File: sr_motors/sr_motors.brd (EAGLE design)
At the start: 78.4 x 64.8 mm, 20 parts

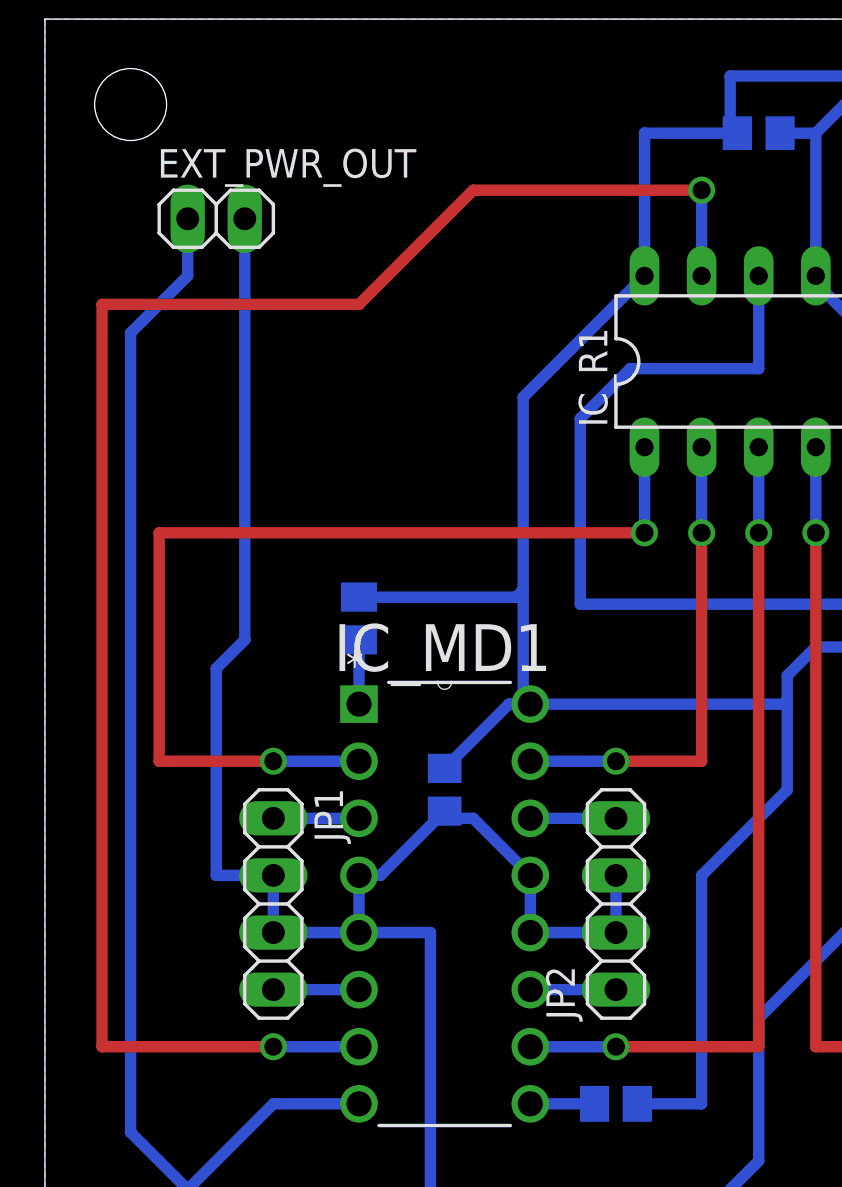
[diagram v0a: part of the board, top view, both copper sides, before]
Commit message: DRC and align: Set the same DRC for lights and motors, fixed new DRC errors in sr_lights, aligned headers
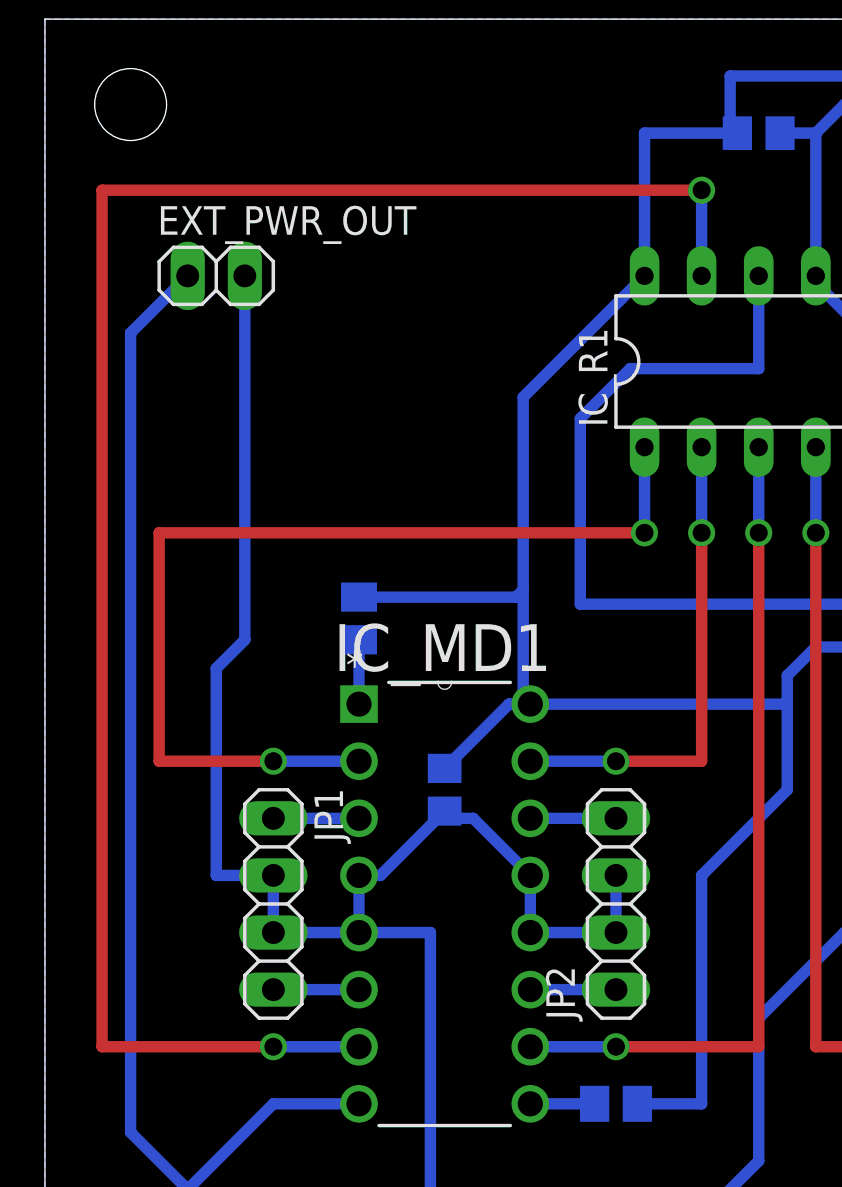
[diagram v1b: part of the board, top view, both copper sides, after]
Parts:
- moved EXT_PWR_OUT 2.54 mm to (7.62, 53.3)
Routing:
- net Q0: track 77.0 -> 80.0 mm
- net VCC2: track 101.8 -> 99.2 mm
- net GND: track 290.3 -> 287.8 mm
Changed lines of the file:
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@@
 </element>
 <element name="EXT_PWR_IN" library="pinhead" package="1X02" value="" x="7.62" y="8.89"/>
-<element name="EXT_PWR_OUT" library="pinhead" package="1X02" value="" x="7.62" y="55.88"/>
+<element name="EXT_PWR_OUT" library="pinhead" package="1X02" value="" x="7.62" y="53.34"/>
 <element name="IC_MD1" library="Texas Instruments_By_element14_Batch_1" package="DIP254P762X508-16" value="L293DNE" x="21.59" y="16.51">
 <attribute name="MPN" value="L293DNE" x="21.59" y="16.51" size="1.778" layer="27" display="off"/>
@@
 <wire x1="69.85" y1="24.13" x2="69.85" y2="53.34" width="0.508" layer="16"/>
 <wire x1="10.16" y1="26.67" x2="10.16" y2="24.13" width="0.508" layer="16"/>
-<wire x1="8.89" y1="37.1475" x2="8.89" y2="55.88" width="0.508" layer="16"/>
+<wire x1="8.89" y1="37.1475" x2="8.89" y2="53.34" width="0.508" layer="16"/>
 <wire x1="7.62" y1="35.8775" x2="8.89" y2="37.1475" width="0.508" layer="16"/>
 <wire x1="7.62" y1="26.67" x2="7.62" y2="35.8775" width="0.508" layer="16"/>
@@
 <wire x1="31.75" y1="13.97" x2="29.21" y2="11.43" width="0.508" layer="16"/>
 <wire x1="29.21" y1="11.43" x2="17.145" y2="11.43" width="0.508" layer="16"/>
-<polygon width="0.4064" layer="16">
+<polygon width="0.508" layer="16">
 <vertex x="0" y="64.77"/>
 <vertex x="78.74" y="64.77"/>
@@
 <via x="29.21" y="57.15" extent="1-16" drill="0.8" shape="square"/>
 <wire x1="10.16" y1="19.05" x2="2.54" y2="19.05" width="0.508" layer="1"/>
-<wire x1="2.54" y1="19.05" x2="2.54" y2="52.07" width="0.508" layer="1"/>
-<wire x1="2.54" y1="52.07" x2="13.97" y2="52.07" width="0.508" layer="1"/>
-<wire x1="13.97" y1="52.07" x2="19.05" y2="57.15" width="0.508" layer="1"/>
-<wire x1="19.05" y1="57.15" x2="29.21" y2="57.15" width="0.508" layer="1"/>
+<wire x1="2.54" y1="19.05" x2="2.54" y2="57.15" width="0.508" layer="1"/>
+<wire x1="2.54" y1="57.15" x2="29.21" y2="57.15" width="0.508" layer="1"/>
 </signal>
 <signal name="Q1">
@@
 <wire x1="16.51" y1="4.1275" x2="29.5275" y2="4.1275" width="0.508" layer="16"/>
 <wire x1="16.51" y1="4.1275" x2="16.51" y2="3.81" width="0.508" layer="16"/>
-<wire x1="6.35" y1="55.88" x2="6.35" y2="53.34" width="0.508" layer="16"/>
 <wire x1="6.35" y1="53.34" x2="3.81" y2="50.8" width="0.508" layer="16"/>
 <wire x1="3.81" y1="50.8" x2="3.81" y2="15.24" width="0.508" layer="16"/>

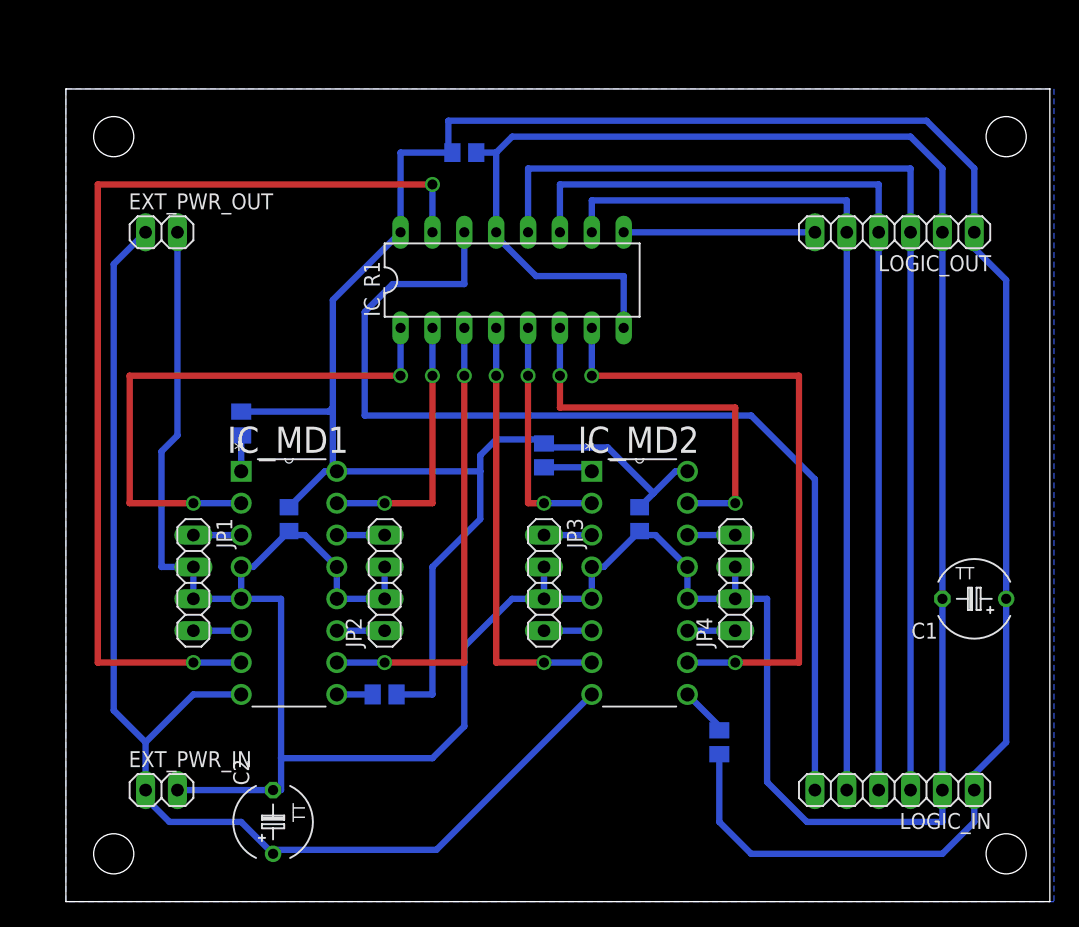
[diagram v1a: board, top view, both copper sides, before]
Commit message: Verion 1.2: Increased route width and board width, small other changes
Squashed commit of the following:

commit cb5b4ae53fc73325e271569d8207a4f4cb0d995e
Author: Sergey Kostyuk <contact@s-kostyuk.me>
Date:   Tue Sep 13 19:34:33 2016 +0300

    Increaded width of routes, increased board width, replaced capacitor package, updated board version

commit 30ef558f6f82cadcaf764826f9decc7df1a17ce0
Author: Sergey Kostyuk <contact@s-kostyuk.me>
Date:   Tue Sep 13 19:27:19 2016 +0300

    Replaced capacitor package

commit a2d398c50457a8d09da237926f830a1984b8064b
Author: Sergey Kostyuk <contact@s-kostyuk.me>
Date:   Tue Sep 13 18:08:38 2016 +0300

    Icreased width of routes, icreased board width

commit f5951c6459f5b93fe179c3fabd85f49e6b5260dd
Author: Sergey Kostyuk <contact@s-kostyuk.me>
Date:   Wed Sep 7 16:51:49 2016 +0300

    Increased width of power lines on sr_motors

commit 1e2f38b3539c2f4abccb8c8183ef937e4e63213c
Author: Sergey Kostyuk <ks.hot.ua@gmail.com>
Date:   Mon Aug 22 15:17:33 2016 +0300

    Added reverse current protection for external power, added version text
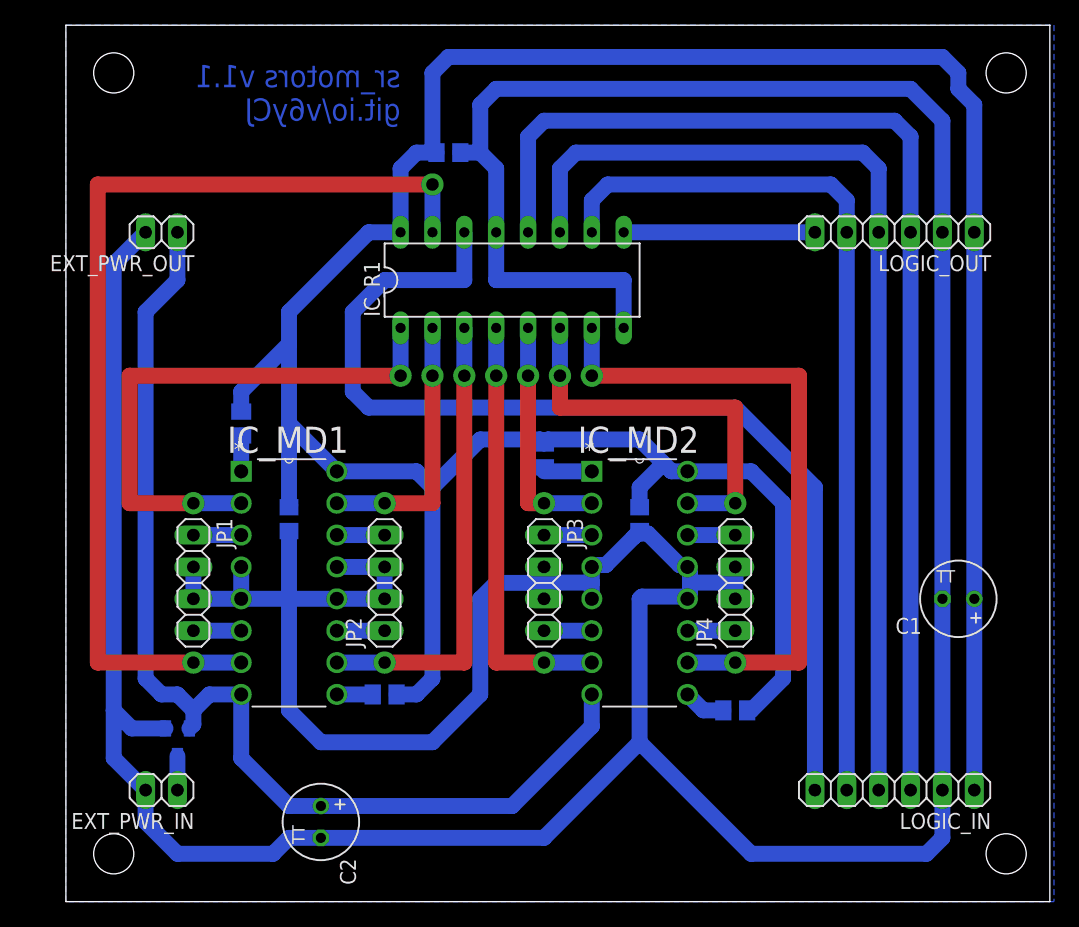
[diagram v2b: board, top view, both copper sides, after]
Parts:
- added Q1: IRLML2244TRPbF, we-transistor:SOT23
- C1, C2: device rcl:TAP5-60 -> rcl:TT2D6
- moved C2 3.81 mm to (20.3, 6.35), turned to 270 degrees
- moved R14 2.84 mm to (53.3, 15.2), turned to 180 degrees
- moved C3 1.27 mm to (30.5, 59.7)
- moved C1 1.27 mm to (71.1, 24.1)
- turned EXT_PWR_IN to 180 degrees
- turned EXT_PWR_OUT to 180 degrees
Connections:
- new net VCC2_RAW: EXT_PWR_IN.1, Q1.3
- net GND: now also Q1.1
- net VCC2: now also Q1.2; no longer EXT_PWR_IN.1
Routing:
- net GND: track 287.8 -> 367.0 mm
- net VCC2: track 99.2 -> 87.2 mm
- net VCC1: track 227.9 -> 235.6 mm
- net RCK: track 85.1 -> 91.2 mm
- net SCK: track 77.5 -> 81.1 mm
- net VCC2_RAW: track 0.00 -> 2.71 mm
- net SCLR: track 69.8 -> 70.9 mm
- net EN3: track 3.91 -> 3.39 mm
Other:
- board size 78.4 x 64.8 mm -> 78.4 x 69.8 mm
- board text added: "sr_motors v1.1 git.io/v6yCJ"
